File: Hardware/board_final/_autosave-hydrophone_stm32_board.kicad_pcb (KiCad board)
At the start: 4 copper layers, 69.8 x 49.9 mm, 98 parts, among them IC1 AD8031ARZ, J1 Conn_01x02, J2 Conn_02x05_Odd_Even, J3 Conn_01x02, J4 Conn_01x04, J5 Micro_SD_Card, J6 142-0701-851, J7 Conn_01x02_Female, U1 AMS1117-3.3, U2 STM32F746ZGT6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

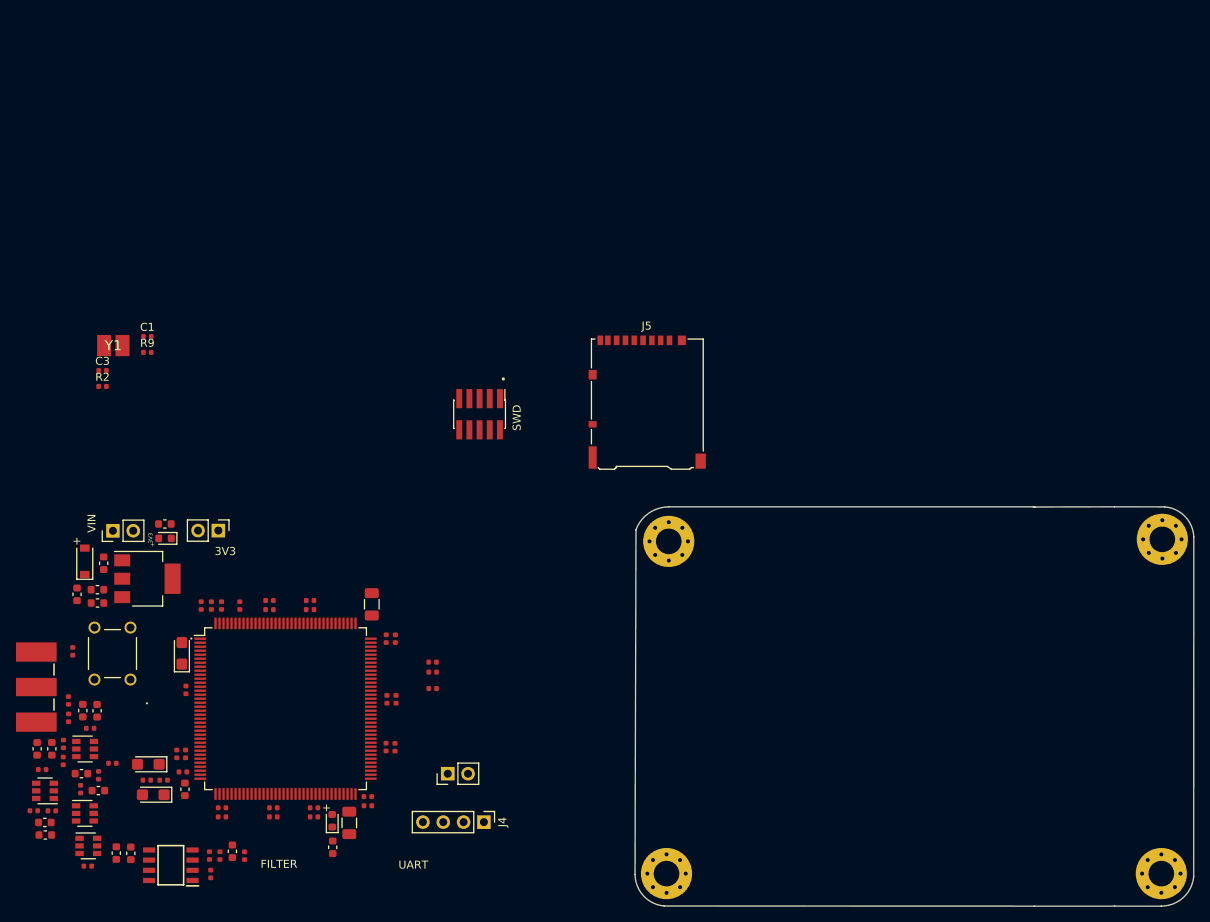
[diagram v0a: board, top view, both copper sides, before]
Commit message: Added F7 100 Pin Version
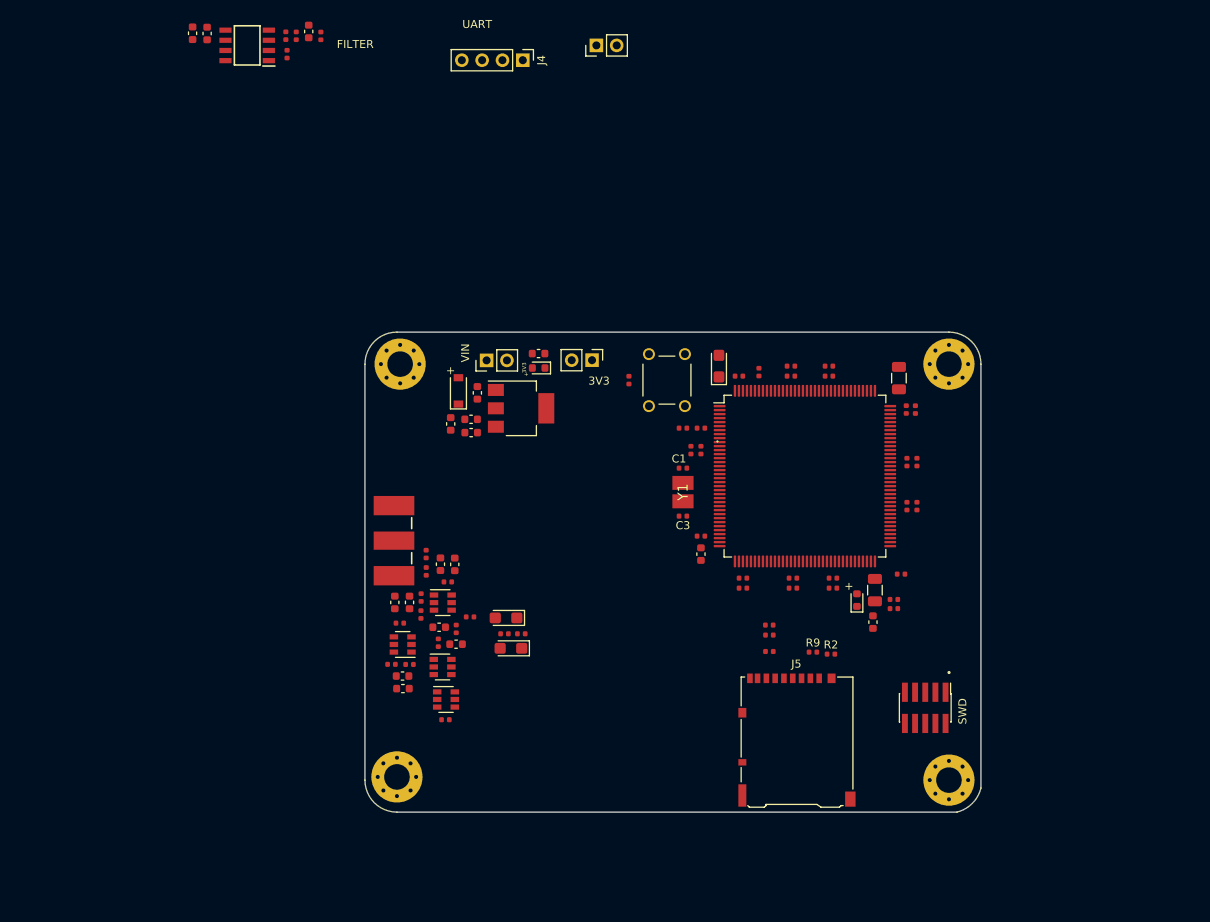
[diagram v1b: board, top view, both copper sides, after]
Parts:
- moved C38 102.9 mm to (66.3, -12.3)
- moved C39 102.9 mm to (64.5, -12.4)
- moved IC1 102.9 mm to (71.3, -10.8)
- moved R16 102.9 mm to (76.3, -9.75)
- moved C40 102.9 mm to (79.0, -12.6)
- moved C41 102.9 mm to (77.4, -12.0)
- moved R14 102.9 mm to (80.5, -12.0)
- moved R15 102.9 mm to (76.1, -12.0)
- moved R2 97.0 mm to (144.2, 65.2)
- moved J4 95.4 mm to (105.7, -8.99)
- moved J7 92.9 mm to (114.9, -10.8)
- moved R9 91.2 mm to (142.0, 65.0)
- moved C11 79.4 mm to (153.0, 55.2)
- moved C7 77.4 mm to (139.5, 55.8)
- moved C27 77.3 mm to (119.0, 31.0)
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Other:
- board size 69.8 x 49.9 mm -> 77 x 60 mm
